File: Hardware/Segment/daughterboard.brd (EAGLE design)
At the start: 210.8 x 51.8 mm, 162 parts, among them IC1 PBQ79656PAPTQ1, IC2 PBQ79656PAPTQ1, T1 PBHV8115X, 115, T2 PBHV8115X, 115

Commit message: Daughterboard PCB arranging work
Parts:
- removed CCB10: 10 nf, rcl:C0603
- removed CCB12, CCB15, CCB37, CCB38, CCB41: 1uf, rcl:C0603
- removed CCB13, CCB20, CCB39, CCB46: 0.1uf, rcl:C0603
- removed CCB14, CCB40: 4.7uf, rcl:C0603
- removed CCB21: 0.22uf, rcl:C0603
- removed CCB26, CCB27, CCB28, CCB29, CCB30, CCB31, CVC10, CVC12, CVC13, CVC14, CVC15, CVC16, CVC17, CVC18: 0.47uf, rcl:C0603
- removed RCB11: 30, rcl:R0603
- removed RCB15, RCB16, RCB17, RCB18, RCB19, RCB20, RCB21, RCB22: 10, rcl:R0603
- removed RVC20, RVC21, RVC22, RVC23, RVC24: 100, rcl:R0603
- removed RVC36: 49, rcl:R0603
- added CAVDD, CAVDD-1, CDVDD, CDVDD-1, CREFHP-1: 1uf, rcl:C0603
- added CBAT: 10 nf, rcl:C0603
- added CCB1-1, CCB2-1, CCB3-1, CCB4-1, CCB5-1, CCB6-1, CVC1-1, CVC3-1, CVC4-1, CVC5-1, CVC6-1, CVC7-1, CVC8-1, CVC9-1: 0.47uf, rcl:C0603
- added CCVDD, CCVDD-1: 4.7uf, rcl:C0603
- added CNEG5V, CNEG5V-1, CNPN2, CNPN2-1: 0.1uf, rcl:C0603
- added CNPN1: 0.22uf, rcl:C0603
- added RBAT: 30, rcl:R0603
- added RCB0-1, RCB10-1, RCB4-1, RCB5-1, RCB6-1, RCB7-1, RCB8-1, RCB9-1: 10, rcl:R0603
- added RNPN-1: 49, rcl:R0603
- added RVC1-1, RVC2-1, RVC3-1, RVC4-1, RVC5-1: 100, rcl:R0603
- moved CCOMH 230.7 mm to (198.1, 38.1)
- moved RCOMHN 230.7 mm to (182.9, 38.1)
- moved RCOMHP 230.7 mm to (190.5, 38.1)
- moved RCOMLP 202.8 mm to (85.1, 3.81)
- moved RCOML 202.8 mm to (100.3, 3.81)
- moved RCOMLN 202.8 mm to (92.7, 3.81)
- moved CCOMLPG 193.1 mm to (106.7, 10.2)
- moved CCOMLP 188.5 mm to (87.6, 14.0)
- moved CCOMLNG 185.1 mm to (106.7, 12.7)
- moved CCOMLN 180.9 mm to (86.4, 10.2)
- moved CCB0 154.5 mm to (59.7, 21.6)
- moved CCB1 154.5 mm to (53.3, 21.6)
- moved CCB2 154.5 mm to (47.0, 21.6)
- moved CCB3 154.5 mm to (40.6, 21.6)
- moved CCB4 154.5 mm to (34.3, 21.6)
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- renumbered C1 to CTSREF1, C2 to CTSREF2, CCB11 to CREFHP, CCB32 to CCB7-1, CCB33 to CCB8-1, CCB34 to CCB9-1, CCB35 to CCB0-1, CCB36 to CBAT-1, CCB47 to CNPN1-1, CVC11 to CVC2-1, CVC19 to CVC0-1, R1 to TEMPR1, R10 to TEMPR10, R11 to TEMPR11, R12 to TEMPR12, R13 to TEMPR13, R14 to TEMPR14, R15 to TEMPR15, R16 to TEMPR16, R2 to TEMPR2, R3 to TEMPR3, R4 to TEMPR4, R5 to TEMPR5, R6 to TEMPR6, R7 to TEMPR7, R8 to TEMPR8, R9 to TEMPR9, RCB12 to RCB1-1, RCB13 to RCB2-1, RCB14 to RCB3-1, RCB23 to RBAT-1, RVC16 to RNPN, RVC25 to RVC6-1, RVC26 to RVC7-1, RVC27 to RVC8-1, RVC28 to RVC9-1, RVC29 to RVC10-1, RVC30 to RVC0-1
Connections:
- net BATC: now also RBAT.2; no longer RCB11.2
- net BATC-1: now also RCB10-1.1, RNPN-1.2; no longer RCB21.1, RVC36.2
- net CVDD: now also CCVDD.2; no longer CCB14.2
- net CVDD-1: now also CCVDD-1.2; no longer CCB40.2
- net GND: now also CAVDD.1, CCVDD.1, CDVDD.1, CNEG5V.1, CNPN1.1; no longer CCB12.1, CCB13.1, CCB14.1, CCB15.1, CCB21.1
- net GND-1: now also CAVDD-1.1, CCVDD-1.1, CDVDD-1.1, CNEG5V-1.1, CREFHP-1.1; no longer CCB37.1, CCB38.1, CCB39.1, CCB40.1, CCB41.1
- net GND1: now also CBAT.1; no longer CCB10.1
- net GND1-1: now also RCB0-1.1; no longer RCB22.1
- net GNDN: now also CNPN2.1; no longer CCB20.1
- net GNDN-1: now also CNPN2-1.1; no longer CCB46.1
- net LDOIN: now also CNPN2.2; no longer CCB20.2
- net LDOIN-1: now also CNPN2-1.2; no longer CCB46.2
- net N$100: now also CVC1-1.2, RVC1-1.1; no longer CVC10.2, RVC20.1
- net N$101: now also CVC1-1.1, RVC2-1.1; no longer CVC10.1, RVC21.1
- net N$102: now also CVC3-1.2, RVC3-1.1; no longer CVC12.2, RVC22.1
- net N$103: now also CVC3-1.1, CVC4-1.2, RVC4-1.1; no longer CVC12.1, CVC13.2, RVC23.1
- net N$104: now also CVC4-1.1, CVC5-1.2, RVC5-1.1; no longer CVC13.1, CVC14.2, RVC24.1
- net N$105: now also CVC5-1.1, CVC6-1.2; no longer CVC14.1, CVC15.2
- net N$106: now also CVC6-1.1, CVC7-1.2; no longer CVC15.1, CVC16.2
- net N$107: now also CVC7-1.1, CVC8-1.2; no longer CVC16.1, CVC17.2
- net N$108: now also CVC8-1.1, CVC9-1.2; no longer CVC17.1, CVC18.2
- net N$109: now also CVC9-1.1; no longer CVC18.1
- net N$111: now also CREFHP-1.2; no longer CCB37.2
- net N$112: now also CAVDD-1.2; no longer CCB38.2
- net N$113: now also CNEG5V-1.2; no longer CCB39.2
- net N$114: now also CDVDD-1.2; no longer CCB41.2
- net N$130: now also RNPN-1.1; no longer RVC36.1
- net N$45: now also CBAT.2, RBAT.1; no longer CCB10.2, RCB11.1
- net N$46: now also CAVDD.2; no longer CCB12.2
- net N$48: now also CNEG5V.2; no longer CCB13.2
- net N$50: now also CDVDD.2; no longer CCB15.2
- net N$65: now also CNPN1.2; no longer CCB21.2
- net N$66: now also RVC1-1.2; no longer RVC20.2
- net N$69: now also CCB1-1.2; no longer CCB26.2
- net N$70: now also RVC2-1.2; no longer RVC21.2
- net N$71: now also CCB1-1.1, CCB2-1.2; no longer CCB26.1, CCB27.2
- net N$74: now also CCB2-1.1, CCB3-1.2; no longer CCB27.1, CCB28.2
- net N$76: now also RVC3-1.2; no longer RVC22.2
- net N$77: now also RVC4-1.2; no longer RVC23.2
- net N$78: now also RCB4-1.1; no longer RCB15.1
- net N$79: now also CCB3-1.1, CCB4-1.2, RCB4-1.2; no longer CCB28.1, CCB29.2, RCB15.2
- net N$80: now also RVC5-1.2; no longer RVC24.2
- net N$81: now also RCB5-1.1; no longer RCB16.1
- net N$82: now also CCB4-1.1, CCB5-1.2, RCB5-1.2; no longer CCB29.1, CCB30.2, RCB16.2
- net N$84: now also RCB6-1.1; no longer RCB17.1
- net N$85: now also CCB5-1.1, CCB6-1.2, RCB6-1.2; no longer CCB30.1, CCB31.2, RCB17.2
- net N$87: now also RCB7-1.1; no longer RCB18.1
- net N$88: now also CCB6-1.1, RCB7-1.2; no longer CCB31.1, RCB18.2
- net N$90: now also RCB8-1.1; no longer RCB19.1
- net N$91: now also RCB8-1.2; no longer RCB19.2
- net N$93: now also RCB9-1.1; no longer RCB20.1
- net N$94: now also RCB9-1.2; no longer RCB20.2
- net N$96: now also RCB10-1.2; no longer RCB21.2
- net N$98: now also RCB0-1.2; no longer RCB22.2

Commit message: Worked on daughterboard PCB
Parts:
- moved CBAT-1 300.7 mm to (218.4, 27.9)
- moved CCB0-1 300.7 mm to (226.1, 27.9)
- moved CCB7-1 300.7 mm to (248.9, 27.9)
- moved CCB8-1 300.7 mm to (241.3, 27.9)
- moved CCB9-1 300.7 mm to (233.7, 27.9)
- moved CCOMHN 296.6 mm to (222.2, 35.6)
- moved CCOMHNG 296.6 mm to (214.6, 35.6)
- moved CCOMHP 296.6 mm to (229.9, 35.6)
- moved CCOMHPG 296.6 mm to (237.5, 35.6)
- moved CNPN1-1 296.6 mm to (245.1, 35.6)
- moved CVC2-1 282.8 mm to (215.9, 16.5)
- moved RVC0-1 278.4 mm to (179.1, 5.08)
- moved RVC10-1 278.4 mm to (186.7, 5.08)
- moved RVC6-1 278.4 mm to (217.2, 5.08)
- moved RVC7-1 278.4 mm to (209.6, 5.08)
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
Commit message: Worked on daughterboard CB/VC L
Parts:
- RCB0, RCB0-1, RCB1, RCB1-1, RCB10, RCB10-1, RCB2, RCB2-1, RCB3, RCB3-1, RCB4, RCB4-1, RCB5, RCB5-1, RCB6, RCB6-1, RCB7, RCB7-1, RCB8, RCB8-1, RCB9, RCB9-1: device rcl:R0603 -> rcl:R1210
- moved TEMPR16 260.1 mm to (165.1, 11.4)
- moved TEMPR15 251.9 mm to (161.3, 11.4)
- moved TEMPR11 248.1 mm to (146.1, 11.4)
- moved TEMPR13 237.8 mm to (156.2, 11.4)
- moved CTSREF2 229.0 mm to (170.2, 10.2)
- moved TEMPR12 228.5 mm to (151.1, 11.4)
- moved TEMPR14 220.4 mm to (132.1, 11.4)
- moved TEMPR10 214.7 mm to (141.0, 11.4)
- moved TEMPR9 194.7 mm to (135.9, 11.4)
- moved RCB10 157.4 mm to (52.1, 21.6), turned to 90 degrees
- moved CTSREF1 118.1 mm to (63.5, 39.4)
- moved RVC9 99.1 mm to (18.4, 15.2), turned to 90 degrees
- moved TEMPR6 97.0 mm to (54.6, 48.3)
- moved TEMPR8 96.8 mm to (62.2, 48.3)
- moved TEMPR7 96.1 mm to (54.6, 43.2)
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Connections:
- net N$1 renamed VC1
- net N$10 renamed VC4
- net N$11 renamed CB7
- net N$110 renamed VC_CB_HIGH-1
- net N$123 renamed TSREF-1
- net N$13 renamed CB4
- net N$14 renamed VC5
- net N$16 renamed CB5
- net N$17 renamed VC8
- net N$19 renamed CB8
- net N$2 renamed CB1
- net N$20 renamed VC9
- net N$22 renamed CB9
- net N$23 renamed VC10
- net N$24 renamed VC0
- net N$25 renamed CB0
- net N$26 renamed VC6
- net N$28 renamed CB6
- net N$3 renamed VC2
- net N$30 renamed VC7
- net N$32 renamed CB10
- net N$4 renamed CB2
- net N$45 renamed VC_CB_HIGH
- net N$58 renamed TSREF
- net N$66 renamed VC1-1
- net N$69 renamed CB1-1
- net N$7 renamed CB3
- net N$70 renamed VC2-1
- net N$71 renamed CB2-1
- net N$74 renamed CB3-1
- net N$76 renamed VC3-1
- net N$77 renamed VC4-1
- net N$79 renamed CB4-1
- net N$80 renamed VC5-1
- net N$82 renamed CB5-1
- net N$83 renamed VC6-1
- net N$85 renamed CB6-1
- net N$86 renamed VC7-1
- net N$88 renamed CB7-1
- net N$89 renamed VC8-1
- net N$9 renamed VC3
- net N$91 renamed CB8-1
- net N$92 renamed VC9-1
- net N$94 renamed CB9-1
- net N$95 renamed VC10-1
- net N$96 renamed CB10-1
- net N$97 renamed VC0-1
- net N$98 renamed CB0-1
- removed net N$115: IC2.61, TEMPH.1, TEMPR16.2
- removed net N$116: IC2.60, TEMPH.2, TEMPR15.2
- removed net N$117: IC2.59, TEMPH.3, TEMPR14.2
- removed net N$118: IC2.58, TEMPH.4, TEMPR13.2
- removed net N$119: IC2.57, TEMPH.5, TEMPR12.2
- removed net N$120: IC2.56, TEMPH.6, TEMPR11.2
- removed net N$121: IC2.55, TEMPH.7, TEMPR10.2
- removed net N$122: IC2.54, TEMPH.8, TEMPR9.2
- removed net N$47: IC1.61, TEMPL.1, TEMPR8.2
- removed net N$51: IC1.60, TEMPL.2, TEMPR7.2
- removed net N$52: IC1.59, TEMPL.3, TEMPR6.2
- removed net N$53: IC1.58, TEMPL.4, TEMPR5.2
- removed net N$54: IC1.57, TEMPL.5, TEMPR4.2
- removed net N$55: IC1.56, TEMPL.6, TEMPR3.2
- removed net N$56: IC1.55, TEMPL.7, TEMPR2.2
- removed net N$57: IC1.54, TEMPL.8, TEMPR1.2
- new net TEMP1: IC1.61, TEMPL.1, TEMPR1.2
- new net TEMP10: IC2.60, TEMPH.2, TEMPR10.2
- new net TEMP11: IC2.59, TEMPH.3, TEMPR11.2
- new net TEMP12: IC2.58, TEMPH.4, TEMPR12.2
- new net TEMP13: IC2.57, TEMPH.5, TEMPR13.2
- new net TEMP14: IC2.56, TEMPH.6, TEMPR14.2
- new net TEMP15: IC2.55, TEMPH.7, TEMPR15.2
- new net TEMP16: IC2.54, TEMPH.8, TEMPR16.2
- new net TEMP2: IC1.60, TEMPL.2, TEMPR2.2
- new net TEMP3: IC1.59, TEMPL.3, TEMPR3.2
- new net TEMP4: IC1.58, TEMPL.4, TEMPR4.2
- new net TEMP5: IC1.57, TEMPL.5, TEMPR5.2
- new net TEMP6: IC1.56, TEMPL.6, TEMPR6.2
- new net TEMP7: IC1.55, TEMPL.7, TEMPR7.2
- new net TEMP8: IC1.54, TEMPL.8, TEMPR8.2
- new net TEMP9: IC2.61, TEMPH.1, TEMPR9.2

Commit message: Layout L
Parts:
- moved TEMPR3 43.7 mm to (75.6, 39.4), turned to 90 degrees
- moved TEMPR5 41.8 mm to (84.5, 39.4), turned to 90 degrees
- moved TEMPR7 38.3 mm to (92.7, 39.4), turned to 90 degrees
- moved TEMPR2 37.2 mm to (71.1, 39.4), turned to 90 degrees
- moved CTSREF1 36.8 mm to (100.3, 39.4), turned to 270 degrees
- moved TEMPR1 35.6 mm to (67.3, 39.4), turned to 90 degrees
- moved TEMPR8 35.4 mm to (96.5, 39.4), turned to 90 degrees
- moved TEMPR6 34.8 mm to (88.3, 39.4), turned to 90 degrees
- moved TEMPR4 34.3 mm to (80.0, 39.4), turned to 90 degrees
- moved CCVDD 31.9 mm to (88.9, 33.0), turned to 270 degrees
- moved CNEG5V 31.8 mm to (96.5, 29.8), turned to 180 degrees
- moved CAVDD 23.6 mm to (93.3, 18.4), turned to 90 degrees
- moved RCOMLP 17.1 mm to (97.8, 15.2), turned to 90 degrees
- moved CCOMLN 16.6 mm to (102.9, 11.4), turned to 90 degrees
- moved RCOMLN 15.3 mm to (102.9, 15.2), turned to 90 degrees
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
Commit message: Daughterboard layout
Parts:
- removed CCOMH: 1k, rcl:R0603
- added RCOMH: 1k, rcl:R0603
- moved CNPN1-1 128.6 mm to (118.1, 15.2), turned to 180 degrees
- moved CCOMHPG 115.7 mm to (121.9, 29.2)
- moved CCOMHP 111.8 mm to (118.1, 39.4), turned to 270 degrees
- moved CCOMHN 99.8 mm to (122.6, 39.4), turned to 270 degrees
- moved CCOMHNG 96.7 mm to (118.1, 29.2)
- moved CCB7-1 95.3 mm to (153.7, 25.4), turned to 180 degrees
- moved RBAT-1 90.9 mm to (125.7, 17.8), turned to 180 degrees
- moved RNPN-1 90.0 mm to (118.1, 17.8)
- moved CDVDD-1 87.7 mm to (118.1, 20.3)
- moved CCB8-1 83.2 mm to (158.1, 25.4), turned to 180 degrees
- moved CCB0-1 79.6 mm to (146.7, 34.3), turned to 180 degrees
- moved CBAT-1 75.2 mm to (143.5, 21.6), turned to 180 degrees
- moved CNPN2-1 73.7 mm to (109.2, 17.8)
- moved RCOMHP 72.4 mm to (118.1, 35.6), turned to 270 degrees
- moved CCB9-1 71.2 mm to (162.6, 25.4), turned to 180 degrees
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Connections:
- net COMHN: now also COMH.2; no longer COMH.1
- net COMHP: now also COMH.1; no longer COMH.2
- net GND: no longer CAVDD.1, CCOMMLN.2, CCOMMLP.1, CCVDD.1, CDVDD.1, CNEG5V.1, CREFHP.1, IC1.36, IC1.39, IC1.46, IC1.50, IC1.65
- net GND-1: no longer CAVDD-1.1, CCOMMHN.1, CCOMMHP.2, CCVDD-1.1, CDVDD-1.1, CNEG5V-1.1, CREFHP-1.1, IC2.36, IC2.39, IC2.46, IC2.50, IC2.65
- net GNDN: now also CAVDD.1, CCOMMLN.2, CCOMMLP.1, CCVDD.1, CDVDD.1, CNEG5V.1, CREFHP.1, IC1.36, IC1.39, IC1.46, IC1.50, IC1.65
- net GNDN-1: now also CAVDD-1.1, CCOMMHN.1, CCOMMHP.2, CCVDD-1.1, CDVDD-1.1, CNEG5V-1.1, CREFHP-1.1, IC2.36, IC2.39, IC2.46, IC2.50, IC2.65
- net N$131: now also RCOMH.2; no longer CCOMH.1
- net N$132: now also RCOMH.1; no longer CCOMH.2

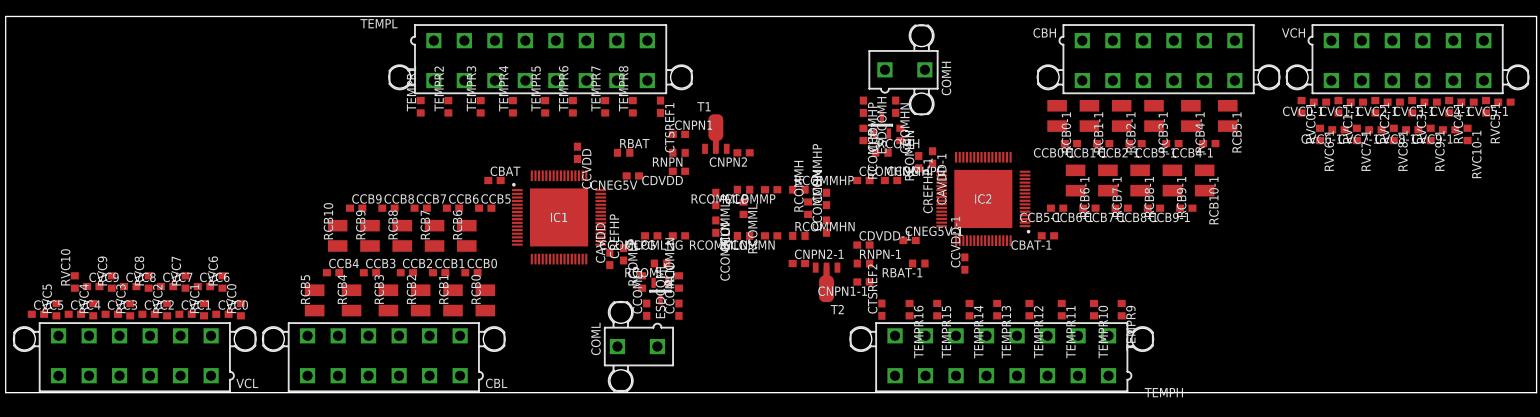
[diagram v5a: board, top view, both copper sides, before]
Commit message: Worked on routing daughterboard, mostly finished COM
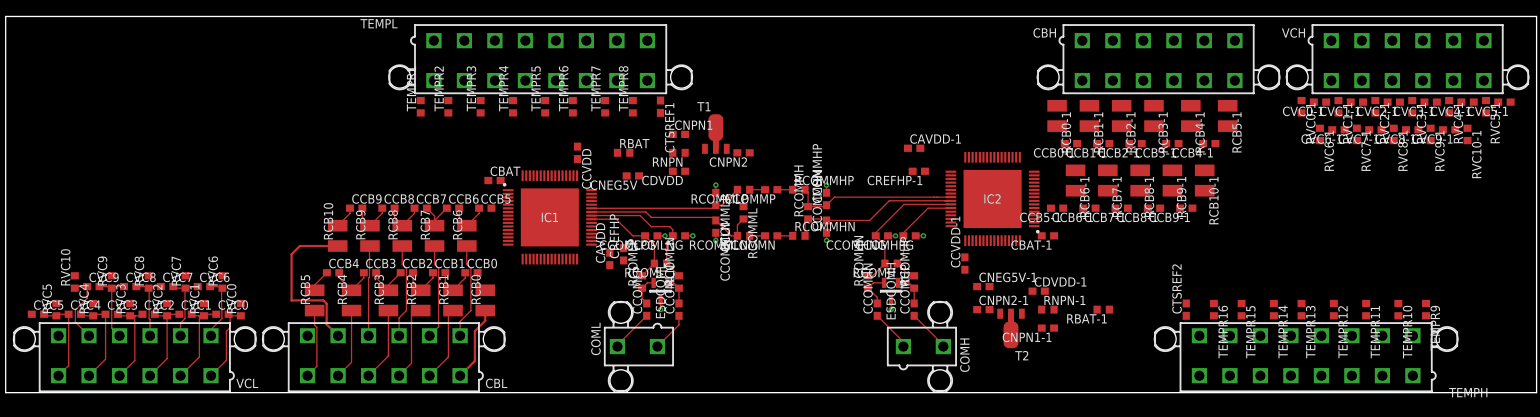
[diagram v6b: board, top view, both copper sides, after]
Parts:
- moved TEMPR9 41.9 mm to (195.6, 11.4)
- moved TEMPR16 41.9 mm to (166.4, 11.4)
- moved CTSREF2 41.9 mm to (162.6, 11.4)
- moved TEMPH 41.9 mm to (179.1, 5.08)
- moved TEMPR10 41.9 mm to (191.8, 11.4)
- moved TEMPR11 41.9 mm to (187.3, 11.4)
- moved TEMPR12 41.9 mm to (182.9, 11.4)
- moved TEMPR13 41.9 mm to (178.4, 11.4)
- moved TEMPR14 41.9 mm to (174.6, 11.4)
- moved TEMPR15 41.9 mm to (170.2, 11.4)
- moved COMH 38.2 mm to (126.4, 6.35)
- moved CCOMHP 28.8 mm to (125.1, 11.4), turned to 90 degrees
- moved CCOMHN 28.1 mm to (120.0, 11.4), turned to 90 degrees
- moved CNPN2-1 26.2 mm to (134.6, 11.4)
- moved T2 26.2 mm to (138.4, 8.89)
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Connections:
- net COMHN: now also COMH.1; no longer COMH.2
- net COMHP: now also COMH.2; no longer COMH.1
- net N$131: now also RCOMH.1; no longer RCOMH.2
- net N$132: now also RCOMH.2; no longer RCOMH.1
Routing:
- net N$59: track 0.00 -> 24.4 mm
- net N$125: track 0.00 -> 24.2 mm
- net N$60: track 0.00 -> 23.8 mm
- net BATC: track 0.00 -> 23.2 mm
- net N$126: track 0.00 -> 22.7 mm
- net N$132: track 0.00 -> 19.8 mm
- net N$29: track 0.00 -> 19.4 mm
- net N$131: track 0.00 -> 15.6 mm
- net N$49: track 0.00 -> 15.1 mm
- net N$27: track 0.00 -> 13.2 mm
- net N$31: track 0.00 -> 13.1 mm
- net N$18: track 0.00 -> 13.0 mm
- net N$38: track 0.00 -> 13.0 mm
- net N$35: track 0.00 -> 12.9 mm
- net N$36: track 0.00 -> 12.8 mm
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
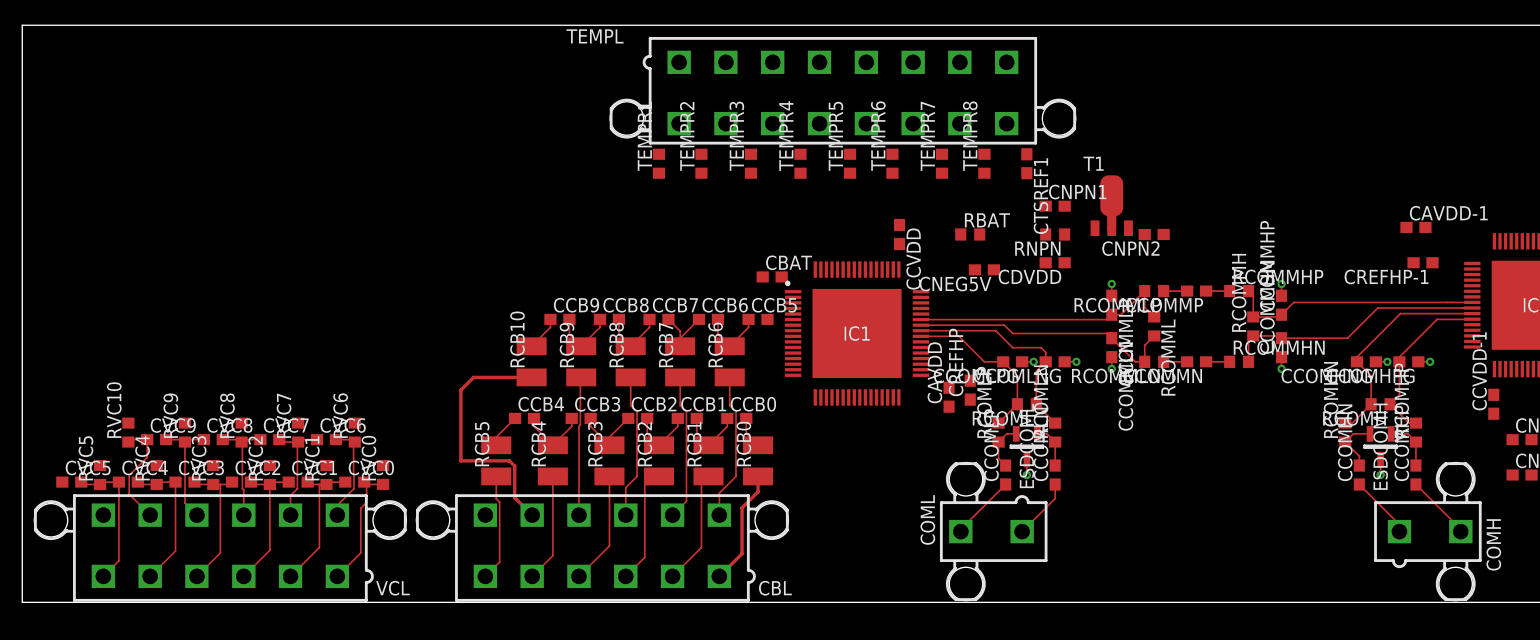
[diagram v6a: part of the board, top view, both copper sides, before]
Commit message: Connected chip 1 (no ground pours yet)
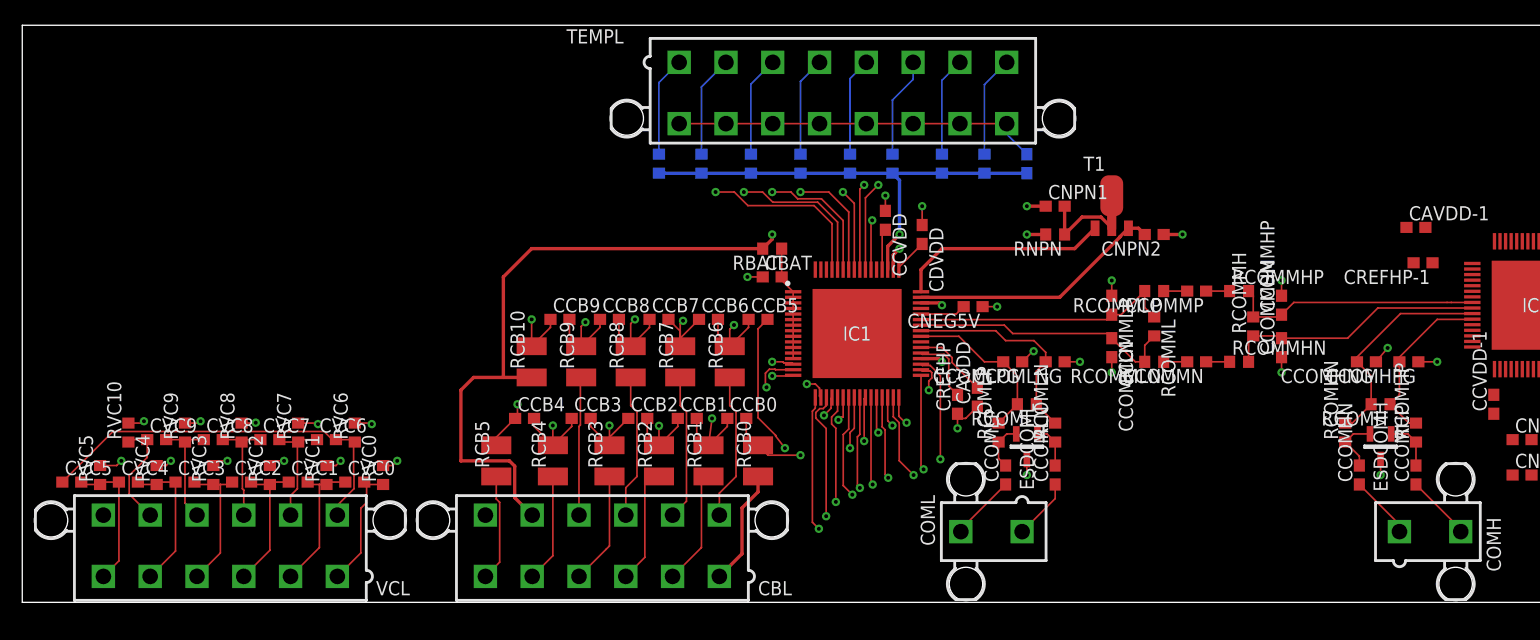
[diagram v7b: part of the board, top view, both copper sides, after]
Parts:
- moved RBAT 17.8 mm to (67.3, 31.8), turned to 180 degrees
- moved CDVDD 12.2 mm to (80.8, 33.0), turned to 270 degrees
- moved CNEG5V 3.45 mm to (85.3, 26.5)
- moved CAVDD 2.54 mm to (85.7, 18.4)
- moved CCVDD 1.80 mm to (77.5, 34.3)
- moved CREFHP 1.71 mm to (83.9, 17.8)
- flipped CTSREF1 to the bottom
- flipped TEMPR1 to the bottom
- flipped TEMPR2 to the bottom
- flipped TEMPR3 to the bottom
- flipped TEMPR4 to the bottom
- flipped TEMPR5 to the bottom
- flipped TEMPR6 to the bottom
- flipped TEMPR7 to the bottom
- flipped TEMPR8 to the bottom
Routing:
- net VC6: track 0.00 -> 108.8 mm, vias 0 -> 2
- net VC7: track 0.00 -> 106.6 mm, vias 0 -> 2
- net VC8: track 0.00 -> 97.7 mm, vias 0 -> 2
- net VC9: track 0.00 -> 94.5 mm, vias 0 -> 2
- net VC5: track 0.00 -> 77.7 mm, vias 0 -> 2
- net VC4: track 0.00 -> 73.2 mm, vias 0 -> 2
- net VC3: track 0.00 -> 68.8 mm, vias 0 -> 2
- net VC2: track 0.00 -> 66.2 mm, vias 0 -> 2
- net VC1: track 0.00 -> 62.6 mm, vias 0 -> 2
- net VC10: track 0.00 -> 62.6 mm, vias 0 -> 2
- net BATC: track 23.2 -> 83.3 mm, vias 0 -> 2
- net VC0: track 0.00 -> 60.0 mm, vias 0 -> 2
- net CB5: track 3.11 -> 53.4 mm, vias 0 -> 3
- net TSREF: track 0.00 -> 42.4 mm, vias 0 -> 1
- net TEMP1: track 0.00 -> 40.0 mm, vias 0 -> 1
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
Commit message: Added com isolation to main board
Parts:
- moved CNEG5V 0.25 mm to (85.3, 26.8)
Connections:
- net GND: no longer CCOMLNG.1, CCOMLPG.1
- net GND-1: no longer CCOMHNG.1, CCOMHPG.1
- net GNDN: now also CCOMLNG.1, CCOMLPG.1
- net GNDN-1: now also CCOMHNG.1, CCOMHPG.1
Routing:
- net GNDN-1: track 2.75 -> 6.07 mm, vias 2 -> 4
- net GND-1: track 4.71 -> 1.39 mm, vias 3 -> 1
- net GNDN: track 18.4 -> 21.3 mm, vias 10 -> 41
- net GND: track 5.88 -> 3.08 mm, vias 4 -> 2
- added copper zone on layer 1, net GNDN
- added copper zone on layer 2, net GNDN
